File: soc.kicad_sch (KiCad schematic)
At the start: 74 parts, among them U1 MPFS250T-FCVG484

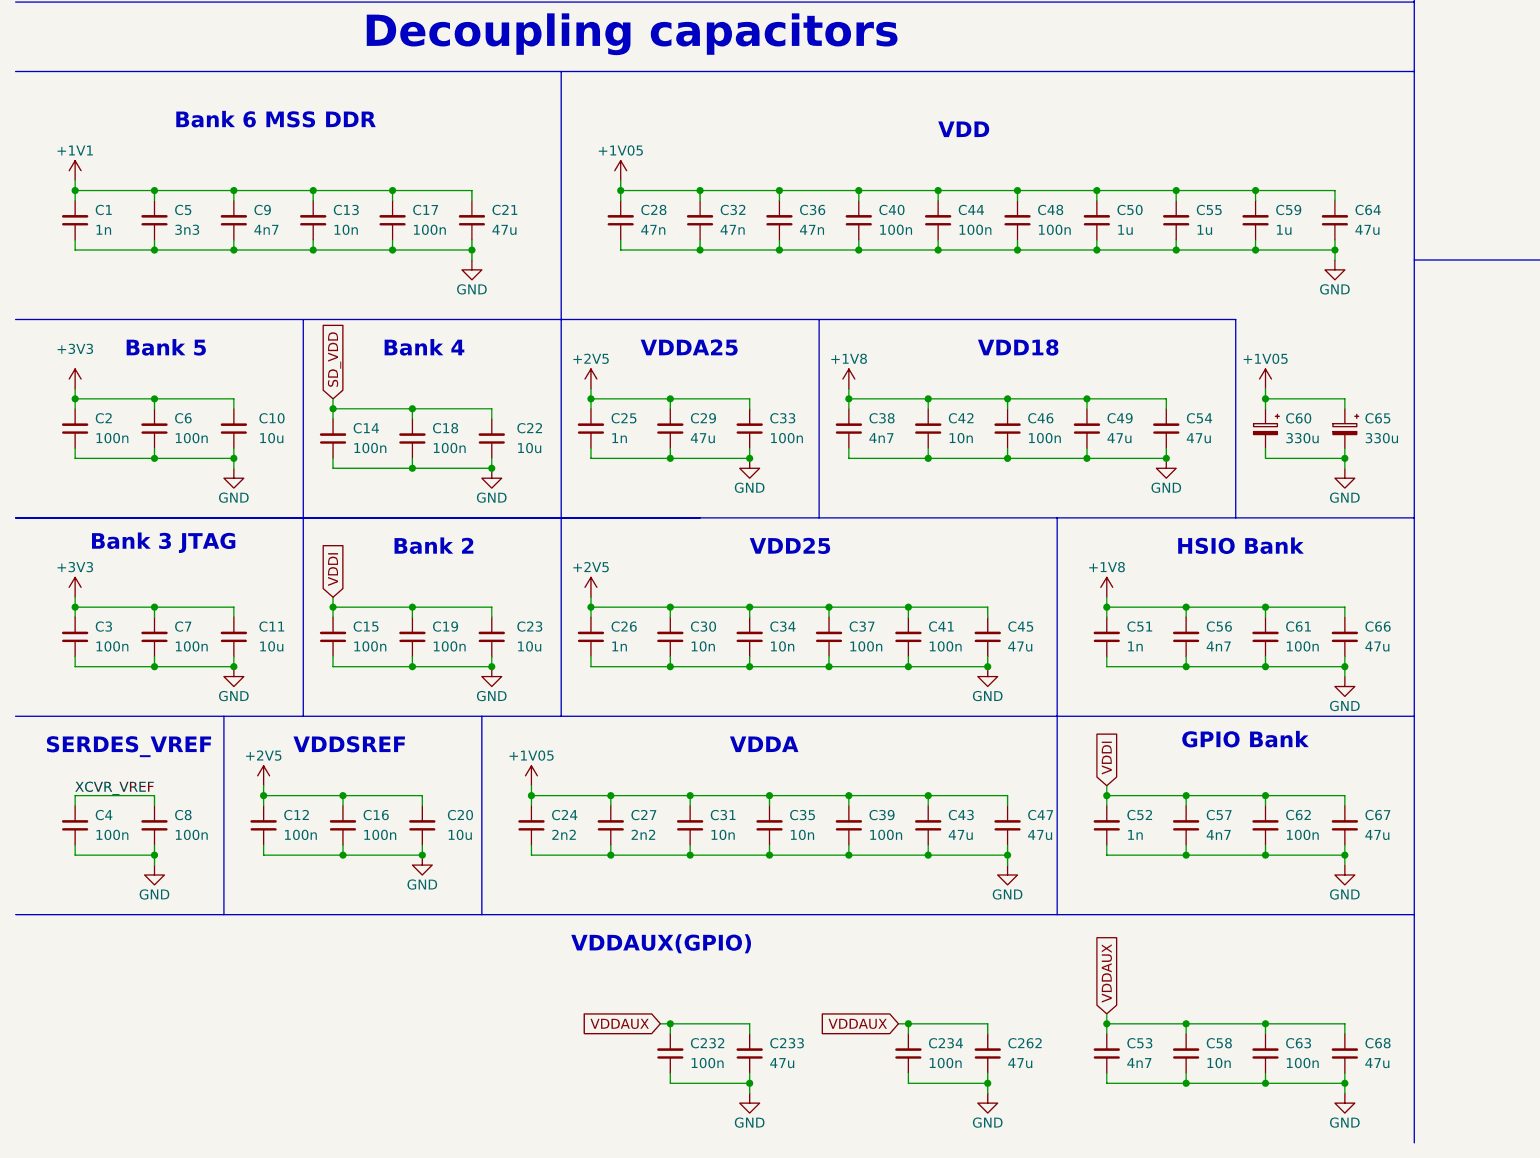
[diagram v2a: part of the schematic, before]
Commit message: [#56060] Reduce decoupling
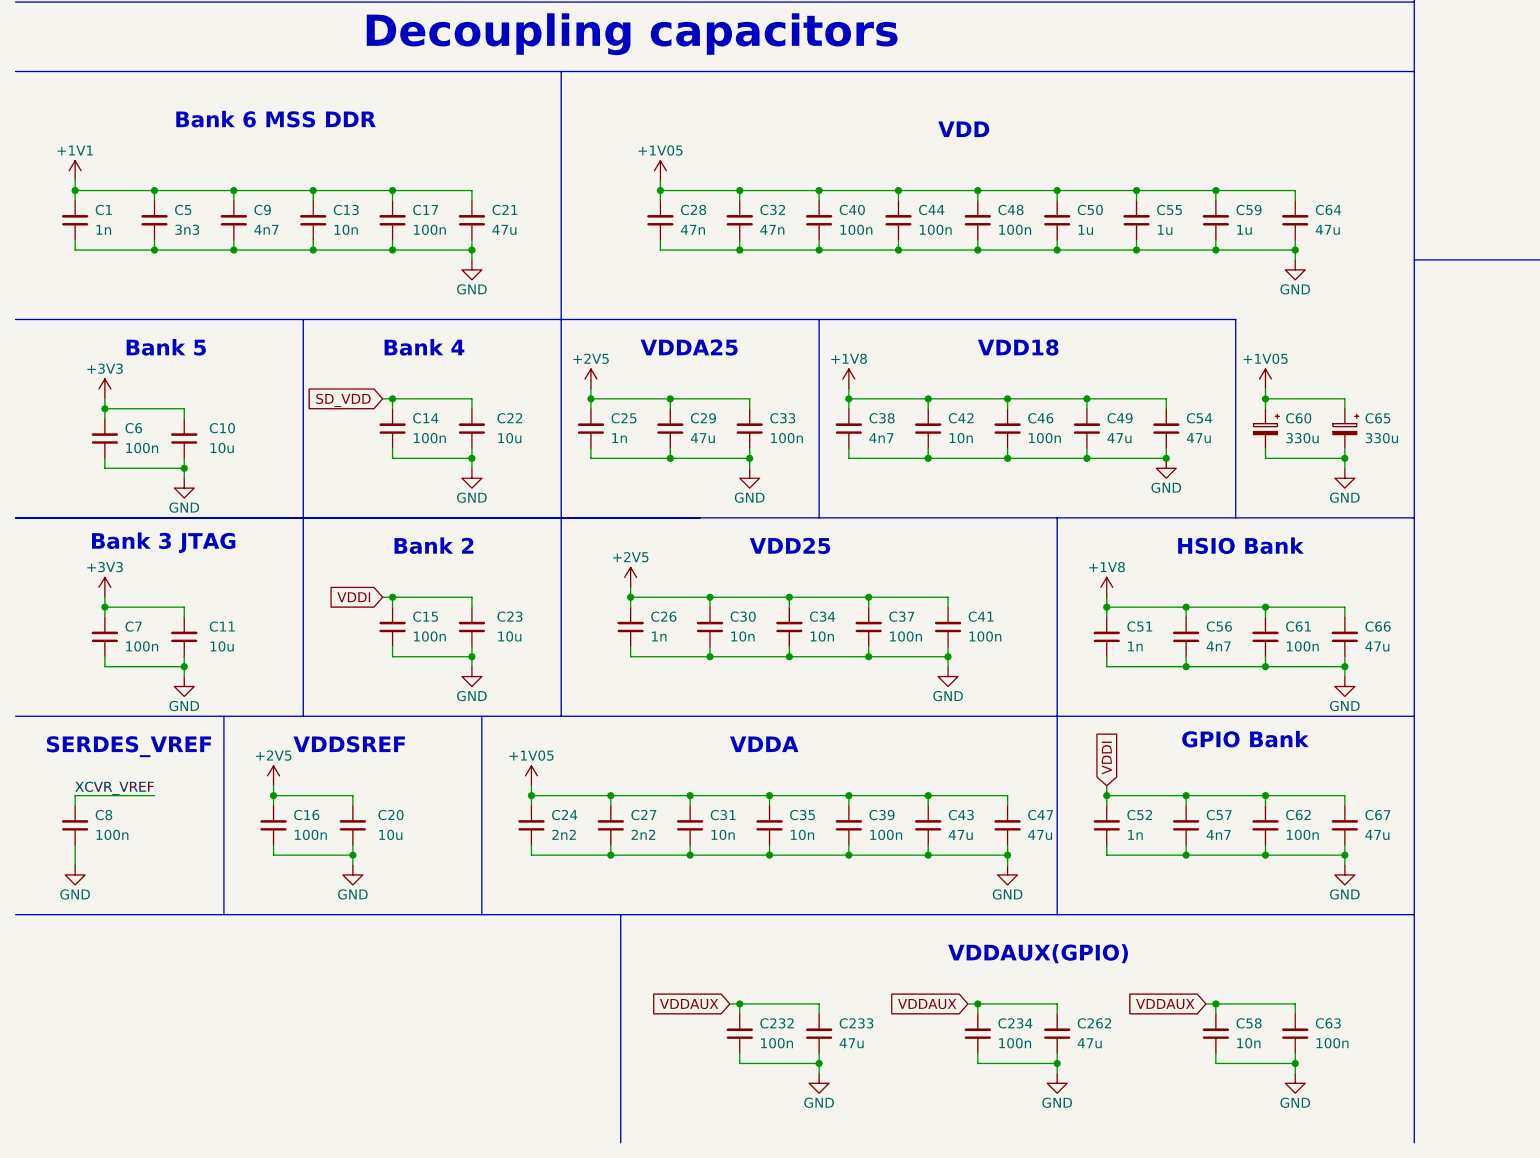
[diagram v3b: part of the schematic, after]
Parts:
- removed C12, C18, C19, C2, C3, C4: C_100n_0402, antmicro-footprints:C_0402_1005Metric, symbol antmicroCapacitors0402:C_100n_0402
- removed C36: C_47n_0402, antmicro-footprints:C_0402_1005Metric, symbol antmicroCapacitors0402:C_47n_0402
- removed C45, C68: C_47u_0603, antmicro-footprints:C_0603_1608Metric, symbol antmicroCapacitors0603:C_47u_0603
- removed C53: C_4n7_0402, antmicro-footprints:C_0402_1005Metric, symbol antmicroCapacitors0402:C_4n7_0402
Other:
- moved on the sheet: C10, C11, C14, C15, C16, C20, C22, C23, C232, C233, C234, C26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

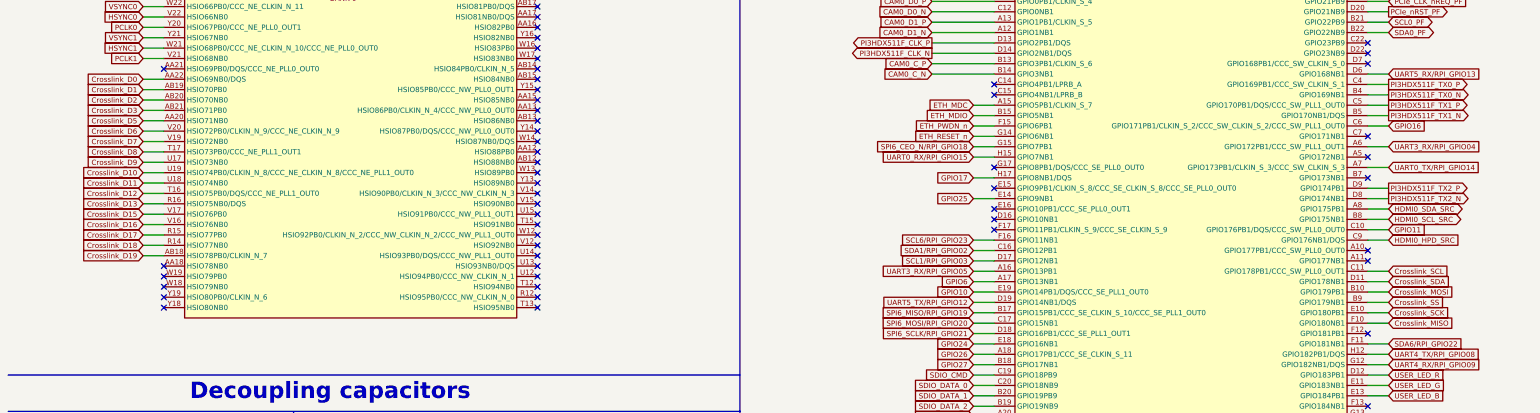
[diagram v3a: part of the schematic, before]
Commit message: [#56466] Update CrossLink's connection
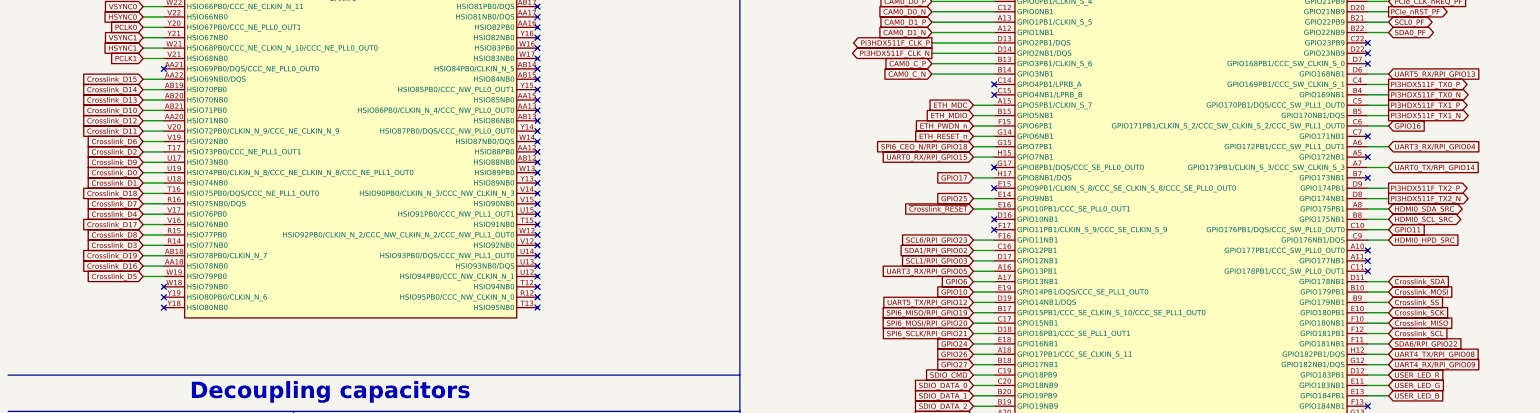
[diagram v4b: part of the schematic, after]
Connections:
- net Crosslink_D0: now also U1.U19 (HSIO74PB0/CLKIN_N_8/CCC_NE_CLKIN_N_8/CCC_NE_PLL1_OUT0); no longer U1.AA22 (HSIO69NB0/DQS)
- net Crosslink_D1: now also U1.U18 (HSIO74NB0); no longer U1.AB19 (HSIO70PB0)
- net Crosslink_D10: now also U1.AB21 (HSIO71PB0); no longer U1.U19 (HSIO74PB0/CLKIN_N_8/CCC_NE_CLKIN_N_8/CCC_NE_PLL1_OUT0)
- net Crosslink_D11: now also U1.V20 (HSIO72PB0/CLKIN_N_9/CCC_NE_CLKIN_N_9); no longer U1.U18 (HSIO74NB0)
- net Crosslink_D12: now also U1.AA20 (HSIO71NB0); no longer U1.T16 (HSIO75PB0/DQS/CCC_NE_PLL1_OUT0)
- net Crosslink_D13: now also U1.AB20 (HSIO70NB0); no longer U1.R16 (HSIO75NB0/DQS)
- net Crosslink_D15: now also U1.AA22 (HSIO69NB0/DQS); no longer U1.V17 (HSIO76PB0)
- net Crosslink_D16: now also U1.AA18 (HSIO78NB0); no longer U1.V16 (HSIO76NB0)
- net Crosslink_D17: now also U1.V16 (HSIO76NB0); no longer U1.R15 (HSIO77PB0)
- net Crosslink_D18: now also U1.T16 (HSIO75PB0/DQS/CCC_NE_PLL1_OUT0); no longer U1.R14 (HSIO77NB0)
- net Crosslink_D2: now also U1.T17 (HSIO73PB0/CCC_NE_PLL1_OUT1); no longer U1.AB20 (HSIO70NB0)
- net Crosslink_D3: now also U1.R14 (HSIO77NB0); no longer U1.AB21 (HSIO71PB0)
- net Crosslink_D5: now also U1.W19 (HSIO79PB0); no longer U1.AA20 (HSIO71NB0)
- net Crosslink_D6: now also U1.V19 (HSIO72NB0); no longer U1.V20 (HSIO72PB0/CLKIN_N_9/CCC_NE_CLKIN_N_9)
- net Crosslink_D7: now also U1.R16 (HSIO75NB0/DQS); no longer U1.V19 (HSIO72NB0)
- net Crosslink_D8: now also U1.R15 (HSIO77PB0); no longer U1.T17 (HSIO73PB0/CCC_NE_PLL1_OUT1)
- net Crosslink_SCL: now also U1.F12 (GPIO181PB1); no longer U1.C11 (GPIO178PB1/CCC_SW_PLL0_OUT1)
- net ~{Crosslink_RESET}: now reaches U1.E16 (GPIO10PB1/CCC_SE_PLL0_OUT1)
- new net Crosslink_D14: U1.AB19 (HSIO70PB0)
- new net Crosslink_D4: U1.V17 (HSIO76PB0)
- no-connect marks 54 -> 51

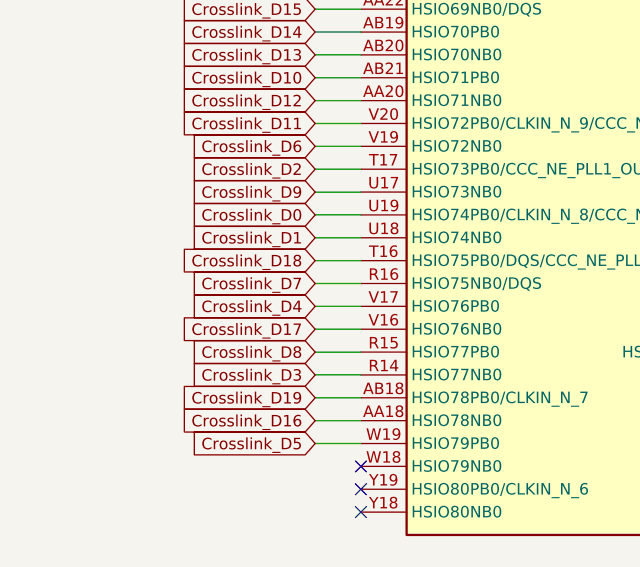
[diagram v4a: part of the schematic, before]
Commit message: [#56715] Match Crosslink bank 1
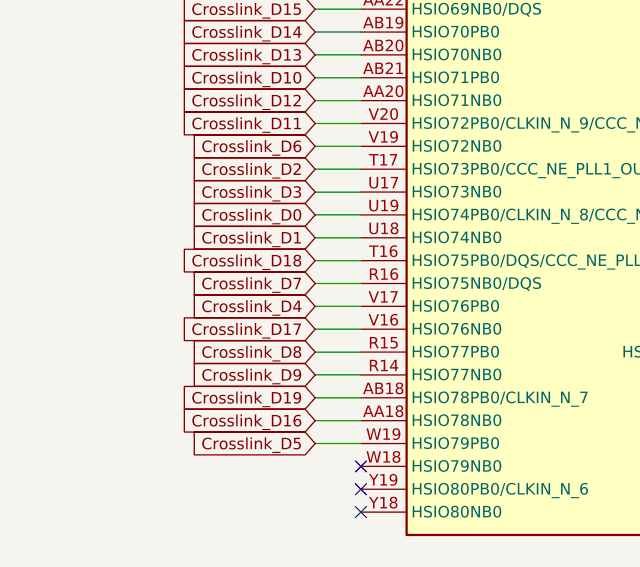
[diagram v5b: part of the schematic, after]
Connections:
- net Crosslink_D3: now also U1.U17 (HSIO73NB0); no longer U1.R14 (HSIO77NB0)
- net Crosslink_D9: now also U1.R14 (HSIO77NB0); no longer U1.U17 (HSIO73NB0)
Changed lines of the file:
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@@
+    )
+  )
+  (global_label "Crosslink_D9" (shape input) (at 45.72 106.68 180) (fields_autoplaced)
+    (effects (font (size 1.27 1.27)) (justify right))
+    (property "Intersheetrefs" "${INTERSHEET_REFS}" (at 31.1512 106.6006 0)
+      (effects (font (size 1.27 1.27)) (justify right) hide)
     )
   )
@@
     )
   )
+  (global_label "Crosslink_D3" (shape input) (at 45.72 86.36 180) (fields_autoplaced)
+    (effects (font (size 1.27 1.27)) (justify right))
+    (property "Intersheetrefs" "${INTERSHEET_REFS}" (at 31.1512 86.2806 0)
+      (effects (font (size 1.27 1.27)) (justify right) hide)
+    )
+  )
   (global_label "Crosslink_D4" (shape input) (at 45.72 99.06 180) (fields_autoplaced)
     (effects (font (size 1.27 1.27)) (justify right))
@@
     )
   )
-  (global_label "Crosslink_D3" (shape input) (at 45.72 106.68 180) (fields_autoplaced)
-    (effects (font (size 1.27 1.27)) (justify right))
-    (property "Intersheetrefs" "${INTERSHEET_REFS}" (at 31.1512 106.6006 0)
-      (effects (font (size 1.27 1.27)) (justify right) hide)
-    )
-  )
   (global_label "CAM0_D0_P" (shape input) (at 238.76 46.99 180) (fields_autoplaced)
     (effects (font (size 1.27 1.27)) (justify right))
@@
     )
   )
-  (global_label "Crosslink_D9" (shape input) (at 45.72 86.36 180) (fields_autoplaced)
-    (effects (font (size 1.27 1.27)) (justify right))
-    (property "Intersheetrefs" "${INTERSHEET_REFS}" (at 31.1512 86.2806 0)
-      (effects (font (size 1.27 1.27)) (justify right) hide)
-    )
-  )
